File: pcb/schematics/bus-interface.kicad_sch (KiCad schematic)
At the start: 51 parts

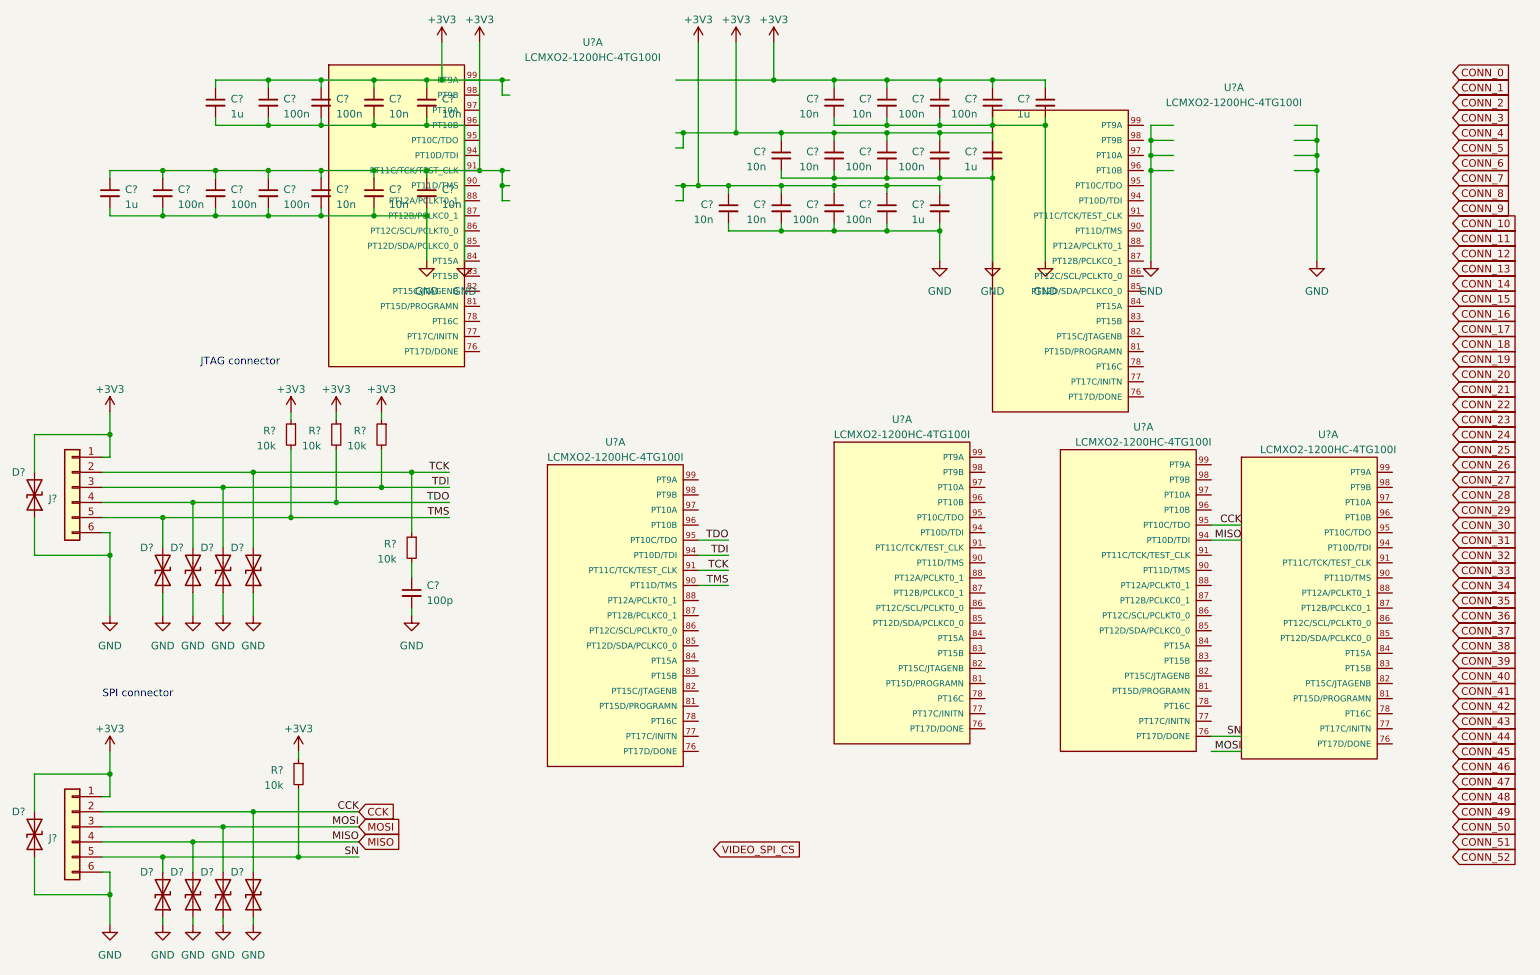
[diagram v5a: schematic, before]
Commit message: add global symbals to the video controller
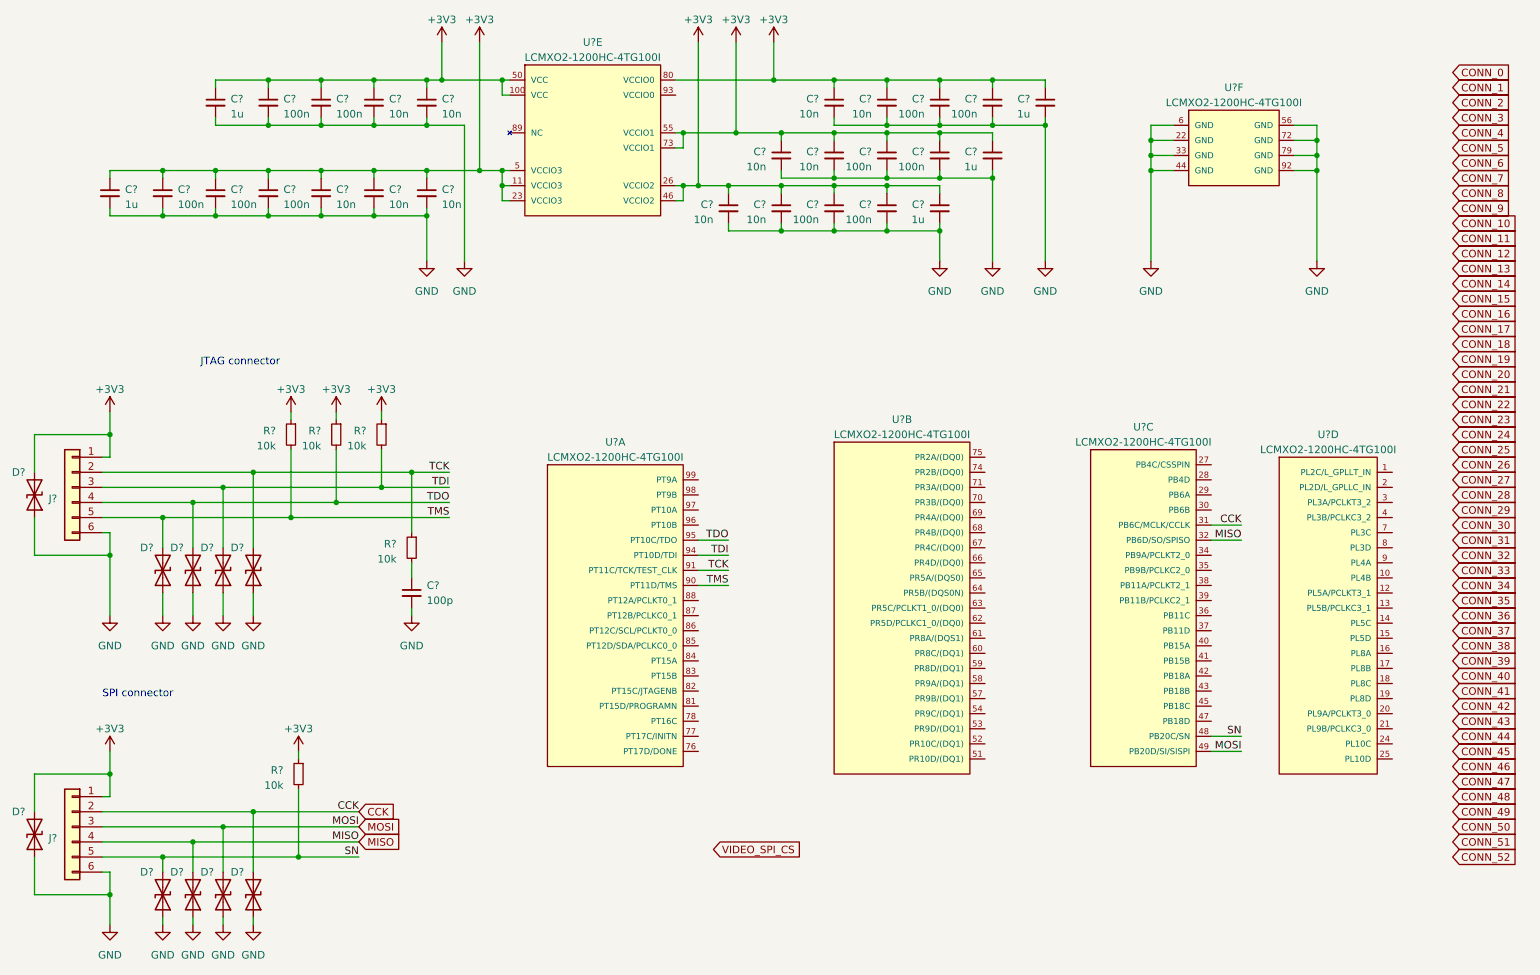
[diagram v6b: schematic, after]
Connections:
- net +3V3: now also U?.100 (VCC), U?.11 (VCCIO3), U?.23 (VCCIO3), U?.26 (VCCIO2), U?.46 (VCCIO2), U?.5 (VCCIO3), U?.50 (VCC), U?.55 (VCCIO1), U?.73 (VCCIO1), U?.80 (VCCIO0); no longer U?.91 (PT11C/TCK/TEST_CLK)
- net CCK: now also U?.31 (PB6C/MCLK/CCLK); no longer U?.95 (PT10C/TDO)
- net GND: now also U?.22 (GND), U?.33 (GND), U?.44 (GND), U?.56 (GND), U?.6 (GND), U?.72 (GND), U?.79 (GND), U?.92 (GND)
- net MISO: now also U?.32 (PB6D/SO/SPISO); no longer U?.94 (PT10D/TDI)
- net MOSI: now also U?.49 (PB20D/SI/SISPI)
- net SN: now also U?.48 (PB20C/SN); no longer U?.76 (PT17D/DONE)

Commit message: choose components and add footprints
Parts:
- C10, C11, C15, C16, C24, C25, C26, C27, C28, C8, C9: renamed from C?; footprint (none) -> Capacitor_SMD:C_0402_1005Metric; Part Number (none) -> C0402C103K5RAC7411
- C12, C13, C17, C18, C21, C22, C23, C29, C30, C6, C7: renamed from C?; footprint (none) -> Capacitor_SMD:C_0603_1608Metric; Part Number (none) -> EMK107B7104KA-T
- C14, C19, C20, C31, C5: renamed from C?; footprint (none) -> Capacitor_SMD:C_0805_2012Metric; Part Number (none) -> 885012207022
- C32: renamed from C?; footprint (none) -> Capacitor_SMD:C_0402_1005Metric; Part Number (none) -> C0402C101J5RACTU
- D1, D10, D2, D3, D4, D5, D6, D7, D8, D9: renamed from D?; footprint (none) -> Diode_SMD:D_0603_1608Metric; Part Number (none) -> 82356240030
- J3, J4: renamed from J?; footprint (none) -> Connector:Tag-Connect_TC2030-IDC-FP_2x03_P1.27mm_Vertical
- R2, R3, R4, R5, R6: renamed from R?; footprint (none) -> Resistor_SMD:R_0603_1608Metric; Part Number (none) -> RC0603JR-0710KL
- U3: renamed from U?; footprint Lattice_Semiconductor-LCMXO2-1200HC-4TG100I-* -> LCMXO2-1200HC-4TG100I:Lattice_Semiconductor-LCMXO2-1200HC-4TG100I-Level_C; Part Number (none) -> LCMXO2-1200HC-4TG100I

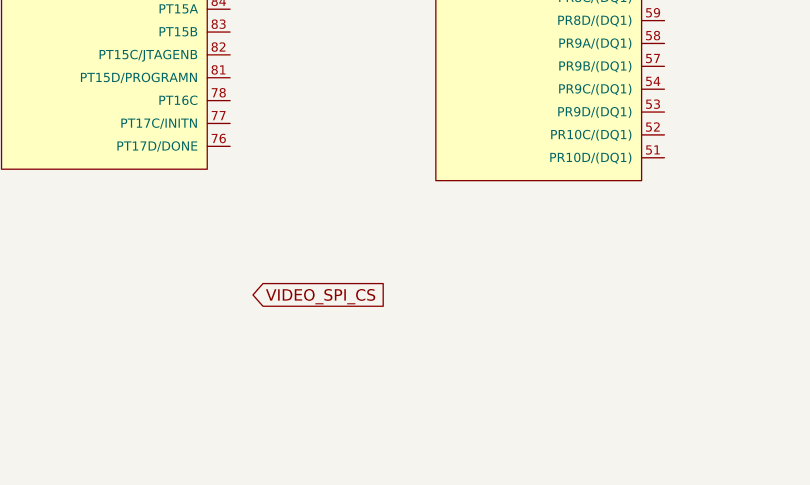
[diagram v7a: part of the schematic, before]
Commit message: add video controller oscillator
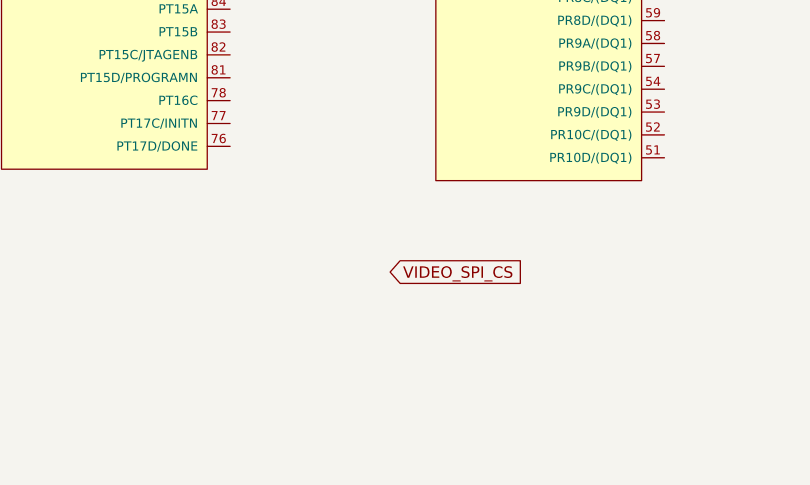
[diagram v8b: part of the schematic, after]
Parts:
- J3, J4: footprint Connector:Tag-Connect_TC2030-IDC-FP_2x03_P1.27mm_Vertical -> Connector:Tag-Connect_TC2030-IDC-NL_2x03_P1.27mm_Vertical
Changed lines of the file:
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@@
     )
   )
-  (global_label "VIDEO_SPI_CS" (shape input) (at 139.7 166.37 0) (fields_autoplaced)
+  (global_label "VIDEO_SPI_CS" (shape input) (at 154.94 163.83 0) (fields_autoplaced)
     (effects (font (size 1.27 1.27)) (justify left))
-    (property "Intersheetrefs" "${INTERSHEET_REFS}" (id 0) (at 155.484 166.37 0)
+    (property "Intersheetrefs" "${INTERSHEET_REFS}" (id 0) (at 170.724 163.83 0)
       (effects (font (size 1.27 1.27)) (justify left))
     )
@@
       (effects (font (size 1.27 1.27)) (justify left) hide)
     )
-    (property "Footprint" "Connector:Tag-Connect_TC2030-IDC-FP_2x03_P1.27mm_Vertical" (id 2) (at 31.75 162.56 0)
+    (property "Footprint" "Connector:Tag-Connect_TC2030-IDC-NL_2x03_P1.27mm_Vertical" (id 2) (at 31.75 162.56 0)
       (effects (font (size 1.27 1.27)) hide)
     )
@@
       (effects (font (size 1.27 1.27)) (justify left) hide)
     )
-    (property "Footprint" "Connector:Tag-Connect_TC2030-IDC-FP_2x03_P1.27mm_Vertical" (id 2) (at 31.75 105.41 0)
-      (effects (font (size 1.27 1.27)) hide)
-    )
+    (property "Footprint" "Connector:Tag-Connect_TC2030-IDC-NL_2x03_P1.27mm_Vertical" (id 2) (at 31.75 105.41 0)
+      (effects (font (size 1.27 1.27)) hide)
+    )
